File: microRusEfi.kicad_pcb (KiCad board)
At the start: 2 copper layers, 80.6 x 93.7 mm, 242 parts, among them CN14 10nF, CN17 10nF, CN5 10nF, CN6 10nF, J1 USB_B_Micro, J2 Conn_02x05_Odd_Even, J3 Conn_01x02, J4 Conn_02x05_Counter_Clockwise, Q1 IPD30N06S2L-23, SW1 SW_Push, SW2 SW_Push, U1 STM32F407VGT6, U11 IS25LP256D-xM, U2 TLE8888QK, U3 Molex_48_pin, U31 MIC4427, U32 MIC4427, U33 MIC4427, U35 MCP6004, U36 MCP6004, U4 TLE9201SG, U46 MCP6004, U5 LM1117-3.3, U6 W25QxxJVS, U7 XC6206 3.3V, U8 MCP6004, X1 8MHz 20pF, Y2 32768 Hz

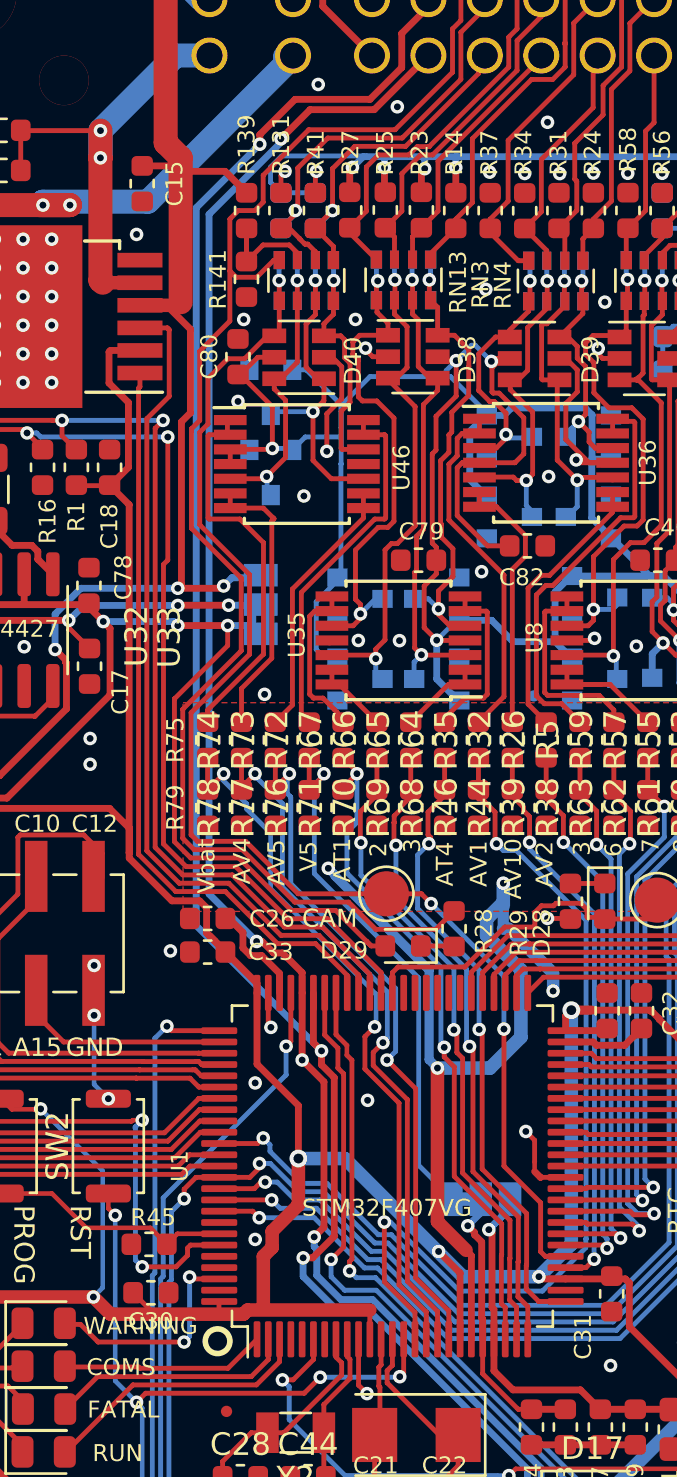
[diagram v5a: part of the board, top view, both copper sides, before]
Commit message: Fix mixed up AV4, AV5, 5Vsense, and 12V sense
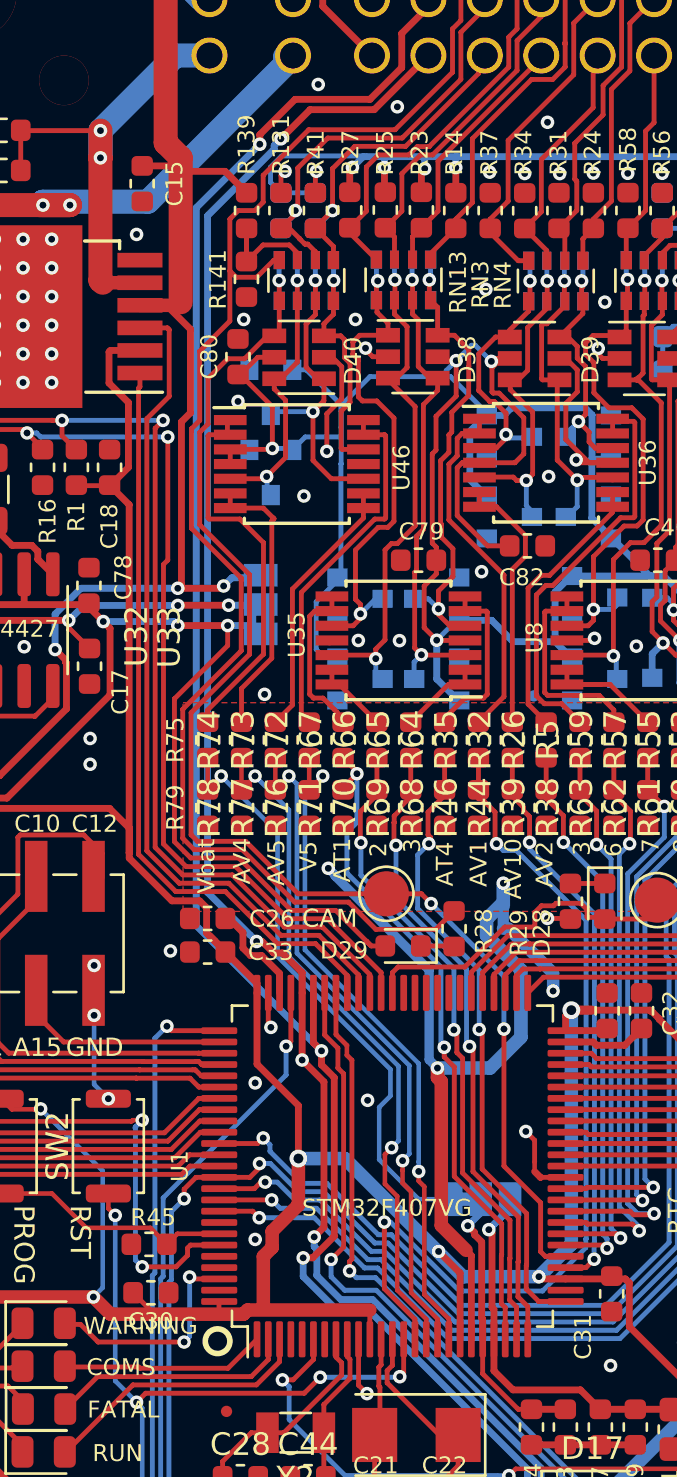
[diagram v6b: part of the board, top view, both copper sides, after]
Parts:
- moved LOGO1 78.4 mm to (45.0, 115.0)
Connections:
- D16 pad 4: (no net) -> Net-(D16-Pad4)
- R72 pad 1: /VSense_ref -> /AV5_MCU
- R73 pad 1: /AV5_MCU -> /AV4_MCU
- R74 pad 1: /AV4_MCU -> /Vbat_MCU
- R75 pad 1: /Vbat_MCU -> /VSense_ref
- R76 pad 2: /VSense_ref -> /AV5_MCU
- R77 pad 2: /AV5_MCU -> /AV4_MCU
- R78 pad 2: /AV4_MCU -> /Vbat_MCU
- R79 pad 2: /Vbat_MCU -> /VSense_ref
- RN6 pad 5: (no net) -> Net-(RN6-Pad5)
- RN6 pad 6: (no net) -> Net-(RN6-Pad6)
- U1 pad 4: (no net) -> /MCU/PE5
- U1 pad 5: (no net) -> /MCU/PE6
- U1 pad 57: (no net) -> /MCU/PD10
- U1 pad 58: (no net) -> /MCU/PD11
- U1 pad 59: (no net) -> /MCU/PD12
- U1 pad 60: (no net) -> /MCU/PD13
- U1 pad 61: (no net) -> /MCU/PD14
- U1 pad 62: (no net) -> /MCU/PD15
- U1 pad 7: (no net) -> /MCU/PC13
- U1 pad 93: (no net) -> /MCU/PB7
- U1 pad 96: (no net) -> /MCU/PB9
- U1 pad 97: (no net) -> /MCU/PE0
- U11 pad 11: (no net) -> Net-(U11-Pad11)
- U11 pad 12: (no net) -> Net-(U11-Pad12)
- U11 pad 13: (no net) -> Net-(U11-Pad13)
- U11 pad 14: (no net) -> Net-(U11-Pad14)
- U11 pad 3: (no net) -> Net-(U11-Pad3)
- U11 pad 4: (no net) -> Net-(U11-Pad4)
- U11 pad 5: (no net) -> Net-(U11-Pad5)
- U11 pad 6: (no net) -> Net-(U11-Pad6)
- U2 pad 17: (no net) -> /TLE8888-1QK/OUT_20
- U2 pad 18: (no net) -> /TLE8888-1QK/OUT_19
- U2 pad 69: (no net) -> /TLE8888-1QK/DFB8
- U2 pad 70: (no net) -> /TLE8888-1QK/DFB9
- U2 pad 71: (no net) -> /TLE8888-1QK/OUT_8
- U2 pad 72: (no net) -> /TLE8888-1QK/OUT_9
- U2 pad 73: (no net) -> /TLE8888-1QK/DFB10
- U2 pad 74: (no net) -> /TLE8888-1QK/OUT_10
- U2 pad 76: (no net) -> Net-(U2-Pad76)
- U2 pad 77: (no net) -> Net-(U2-Pad77)
- U2 pad 78: (no net) -> Net-(U2-Pad78)
- U2 pad 79: (no net) -> Net-(U2-Pad79)
- U2 pad 80: (no net) -> Net-(U2-Pad80)
- U2 pad 81: (no net) -> Net-(U2-Pad81)
- U31 pad 1: (no net) -> Net-(U31-Pad1)
- U31 pad 8: (no net) -> Net-(U31-Pad8)
- U32 pad 1: (no net) -> Net-(U32-Pad1)
- U32 pad 8: (no net) -> Net-(U32-Pad8)
- U33 pad 1: (no net) -> Net-(U33-Pad1)
- U33 pad 8: (no net) -> Net-(U33-Pad8)
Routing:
- net /VSense_ref: track 23.6 -> 26.5 mm
- net /AV4_MCU: track 31.2 -> 30.2 mm
- net /AV5_MCU: track 30.9 -> 30.2 mm
- net /Vbat_MCU: track 31.5 -> 30.9 mm
